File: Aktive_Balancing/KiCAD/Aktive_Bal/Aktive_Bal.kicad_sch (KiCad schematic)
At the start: 60 parts, among them J1 Screw_Terminal_01x02, J10 Conn_01x01_Pin, J11 Conn_01x01_Pin, J2 A-DF_09_A_KG-T4S, J3 Conn_01x02_Pin, J4 Conn_01x02_Pin, J5 Sockel_BluePill, J6 Conn_01x02_Pin, J7 Conn_01x02_Pin, J8 Conn_01x02_Pin, J9 Conn_01x02_Pin, U1 RFP12N10L, U2 SN65HVD233, U3 ADUM1250ARZ-RL7, U4 SCW20C-12, U5 PCA9306DC, U6 EC1SA16N, U7 PCF8575CDB, U8 LM1117IMPX_3_3_NOPB, U9 MCP4725xxx-xCH

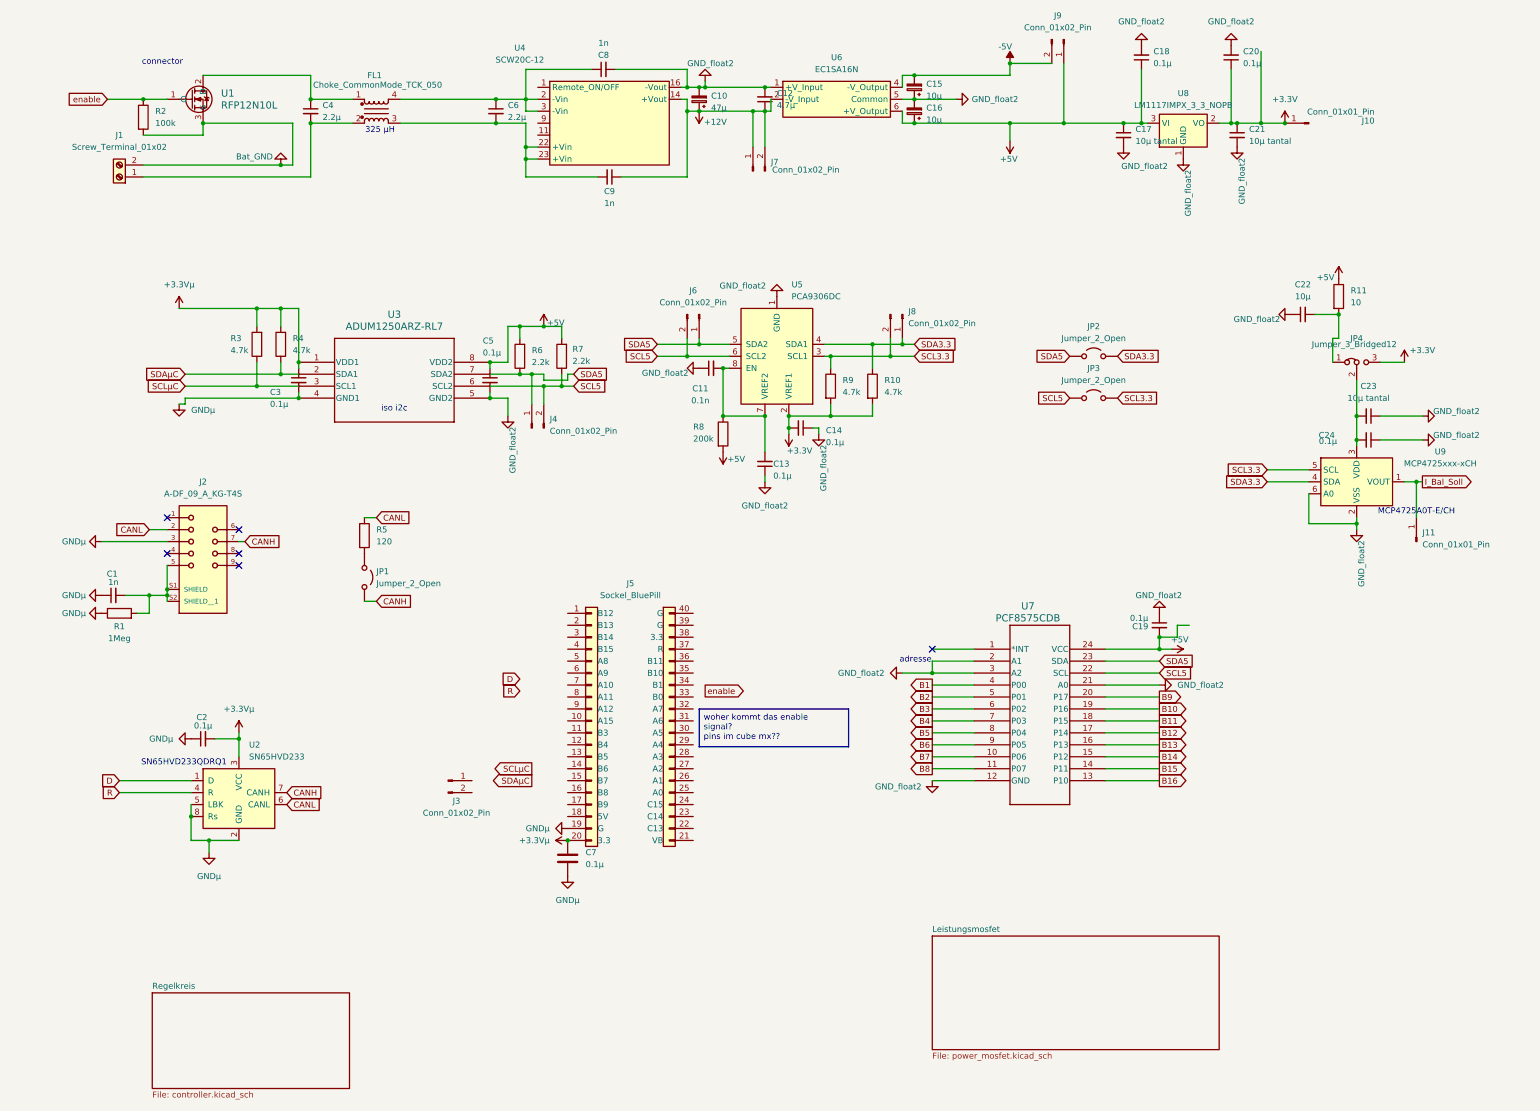
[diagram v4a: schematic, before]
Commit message: layout
Komponenten geordnet
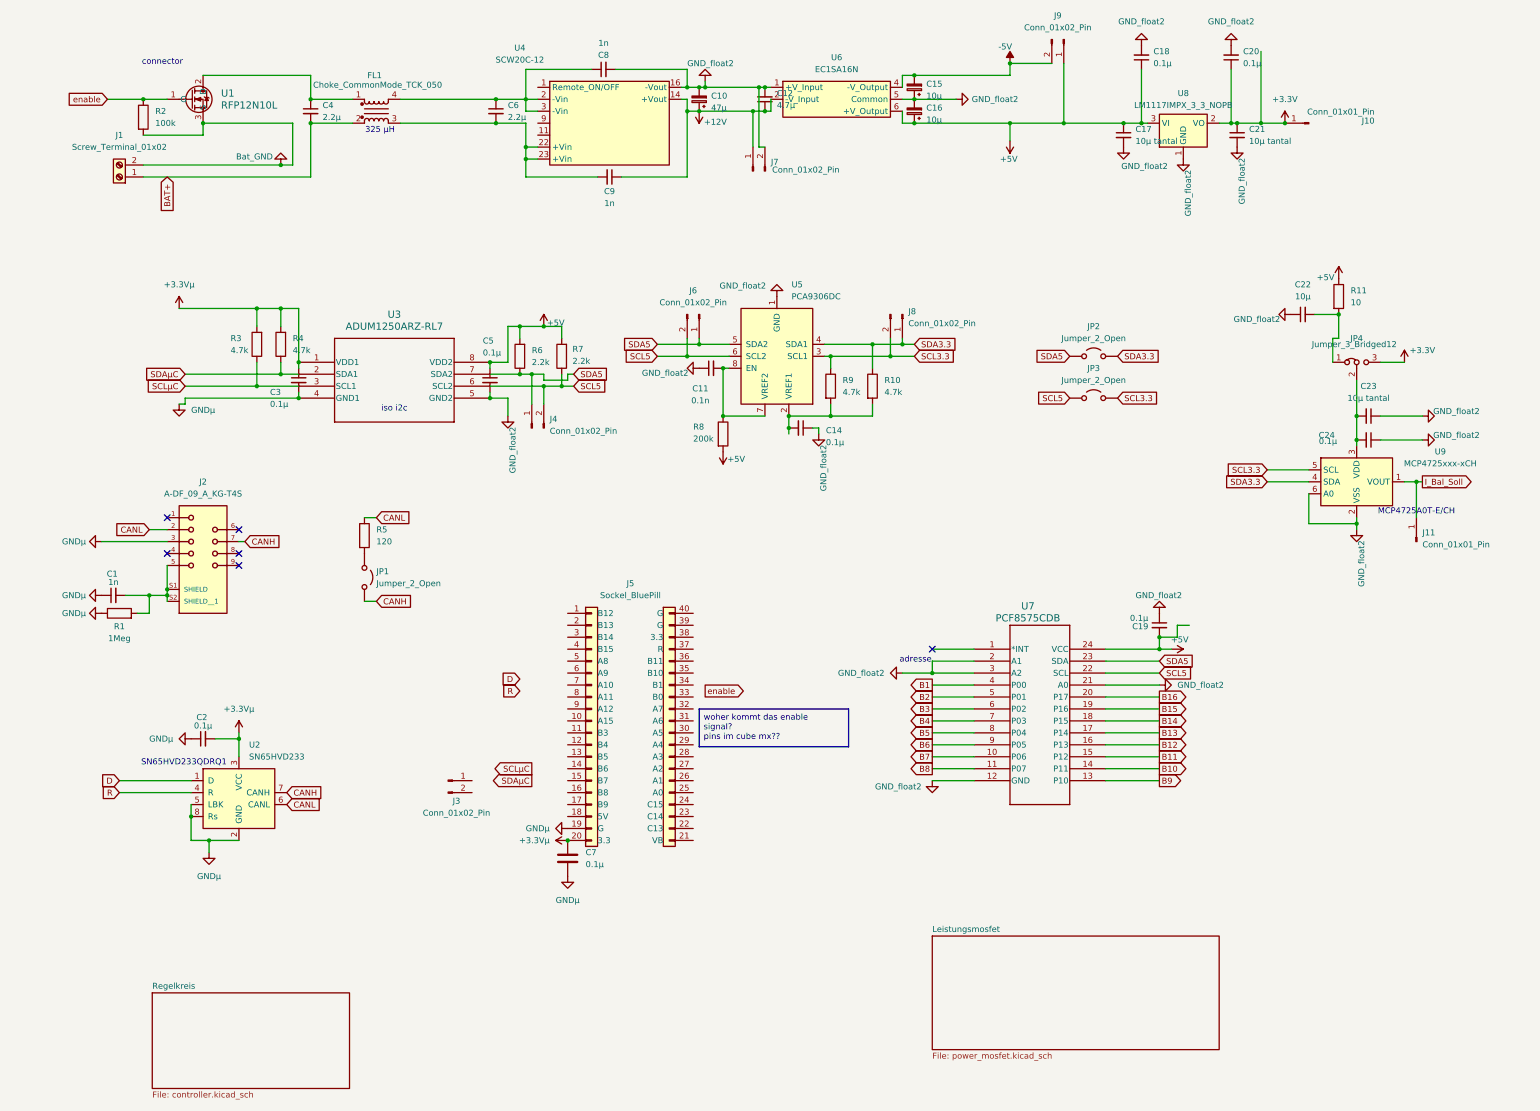
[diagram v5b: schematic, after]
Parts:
- removed C13: 0.1µ, Capacitor_SMD:C_0805_2012Metric, symbol Device:C_Small
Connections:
- net +12V: no longer J7.2 (Pin_2)
- net +3.3V: no longer C14.2, R10.2, R9.2, U5.2 (VREF1)
- net B10: now also U7.14 (P11); no longer U7.19 (P16)
- net B11: now also U7.15 (P12); no longer U7.18 (P15)
- net B12: now also U7.16 (P13); no longer U7.17 (P14)
- net B13: now also U7.17 (P14); no longer U7.16 (P13)
- net B14: now also U7.18 (P15); no longer U7.15 (P12)
- net B15: now also U7.19 (P16); no longer U7.14 (P11)
- net B16: now also U7.20 (P17); no longer U7.13 (P10)
- net B9: now also U7.13 (P10); no longer U7.20 (P17)
- net GND_float2: now also J7.2 (Pin_2)
- net BAT+: now reaches C4.2, FL1.2, J1.1 (Pin_1)
- new net: C14.2, R10.2, R9.2, U5.2 (VREF1)
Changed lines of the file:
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@@
 	)
 	(junction
-		(at 172.72 100.33)
-		(diameter 0)
-		(color 0 0 0 0)
-	)
-	(junction
 		(at 199.39 87.63)
 		(diameter 0)
@@
 		(color 0 0 0 0)
 	)
+	(junction
+		(at 171.45 30.48)
+		(diameter 0)
+		(color 0 0 0 0)
+	)
 	(no_connect
 		(at 45.72 121.92)
@@
 	(wire
 		(pts
-			(xy 172.72 114.3) (xy 172.72 113.03)
-		)
-		(stroke
-			(width 0)
-			(type default)
-		)
-	)
-	(wire
-		(pts
 			(xy 158.75 83.82) (xy 158.75 85.09)
 		)
@@
 	(wire
 		(pts
-			(xy 158.75 30.48) (xy 172.72 30.48)
+			(xy 158.75 30.48) (xy 171.45 30.48)
 		)
 		(stroke
@@
 	(wire
 		(pts
-			(xy 172.72 100.33) (xy 172.72 107.95)
+			(xy 171.45 43.18) (xy 171.45 30.48)
 		)
 		(stroke
@@
 	(wire
 		(pts
+			(xy 171.45 30.48) (xy 172.72 30.48)
+		)
+		(stroke
+			(width 0)
+			(type default)
+		)
+	)
+	(wire
+		(pts
 			(xy 288.29 123.19) (xy 298.45 123.19)
 		)
@@
 	(wire
 		(pts
-			(xy 172.72 35.56) (xy 172.72 43.18)
-		)
-		(stroke
-			(width 0)
-			(type default)
-		)
-	)
-	(wire
-		(pts
 			(xy 49.53 91.44) (xy 69.85 91.44)
 		)
@@
 	(wire
 		(pts
+			(xy 172.72 43.18) (xy 171.45 43.18)
+		)
+		(stroke
+			(width 0)
+			(type default)
+		)
+	)
+	(wire
+		(pts
 			(xy 64.77 88.9) (xy 64.77 93.98)
 		)
@@
 	(global_label "B13"
 		(shape output)
-		(at 256.54 170.18 0)
+		(at 256.54 167.64 0)
 		(fields_autoplaced yes)
 		(effects
@@
 		)
 		(property "Intersheetrefs" "${INTERSHEET_REFS}"
-			(at 263.2142 170.18 0)
+			(at 263.2142 167.64 0)
 			(hide yes)
 			(show_name no)
@@
 	(global_label "B14"
 		(shape output)
-		(at 256.54 172.72 0)
+		(at 256.54 165.1 0)
 		(fields_autoplaced yes)
 		(effects
@@
 		)
 		(property "Intersheetrefs" "${INTERSHEET_REFS}"
-			(at 263.2142 172.72 0)
+			(at 263.2142 165.1 0)
 			(hide yes)
 			(show_name no)
@@
 	(global_label "B12"
 		(shape output)
-		(at 256.54 167.64 0)
+		(at 256.54 170.18 0)
 		(fields_autoplaced yes)
 		(effects
@@
 		)
 		(property "Intersheetrefs" "${INTERSHEET_REFS}"
-			(at 263.2142 167.64 0)
+			(at 263.2142 170.18 0)
 			(hide yes)
 			(show_name no)
@@
 	(global_label "B11"
 		(shape output)
-		(at 256.54 165.1 0)
+		(at 256.54 172.72 0)
 		(fields_autoplaced yes)
 		(effects
@@
 		)
 		(property "Intersheetrefs" "${INTERSHEET_REFS}"
-			(at 263.2142 165.1 0)
+			(at 263.2142 172.72 0)
 			(hide yes)
 			(show_name no)
@@
 		)
 	)
+	(global_label "BAT+"
+		(shape input)
+		(at 45.72 49.53 270)
+		(fields_autoplaced yes)
+		(effects
+			(font
+				(size 1.27 1.27)
+			)
+			(justify right)
+		)
+		(property "Intersheetrefs" "${INTERSHEET_REFS}"
+			(at 45.72 57.4138 90)
+			(hide yes)
+			(show_name no)
+			(do_not_autoplace no)
+			(effects
+				(font
+					(size 1.27 1.27)
+				)
+				(justify right)
+			)
+		)
+	)
 	(global_label "SCL3.3"
 		(shape input)
@@
 	(global_label "B16"
 		(shape output)
-		(at 256.54 177.8 0)
+		(at 256.54 160.02 0)
 		(fields_autoplaced yes)
 		(effects
@@
 		)
 		(property "Intersheetrefs" "${INTERSHEET_REFS}"
-			(at 263.2142 177.8 0)
+			(at 263.2142 160.02 0)
 			(hide yes)
 			(show_name no)
@@
 	(global_label "B15"
 		(shape output)
-		(at 256.54 175.26 0)
+		(at 256.54 162.56 0)
 		(fields_autoplaced yes)
 		(effects
@@
 		)
 		(property "Intersheetrefs" "${INTERSHEET_REFS}"
-			(at 263.2142 175.26 0)
+			(at 263.2142 162.56 0)
 			(hide yes)
 			(show_name no)
@@
 	(global_label "B10"
 		(shape output)
-		(at 256.54 162.56 0)
+		(at 256.54 175.26 0)
 		(fields_autoplaced yes)
 		(effects
@@
 		)
 		(property "Intersheetrefs" "${INTERSHEET_REFS}"
-			(at 263.2142 162.56 0)
+			(at 263.2142 175.26 0)
 			(hide yes)
 			(show_name no)
@@
 	(global_label "B9"
 		(shape output)
-		(at 256.54 160.02 0)
+		(at 256.54 177.8 0)
 		(fields_autoplaced yes)
 		(effects
@@
 		)
 		(property "Intersheetrefs" "${INTERSHEET_REFS}"
-			(at 262.0047 160.02 0)
+			(at 262.0047 177.8 0)
 			(hide yes)
 			(show_name no)
@@
 	)
 	(symbol
-		(lib_id "power:GND")
-		(at 172.72 114.3 0)
-		(unit 1)
-		(body_style 1)
-		(exclude_from_sim no)
-		(in_bom yes)
-		(on_board yes)
-		(in_pos_files yes)
-		(dnp no)
-		(fields_autoplaced yes)
-		(property "Reference" "#PWR019"
-			(at 172.72 120.65 0)
-			(hide yes)
-			(show_name no)
-			(do_not_autoplace no)
-			(effects
-				(font
-					(size 1.27 1.27)
-				)
-			)
-		)
-		(property "Value" "GND_float2"
-			(at 172.72 119.38 0)
-			(show_name no)
-			(do_not_autoplace no)
-			(effects
-				(font
-					(size 1.27 1.27)
-				)
-			)
-		)
-		(property "Footprint" ""
-			(at 172.72 114.3 0)
-			(hide yes)
-			(show_name no)
-			(do_not_autoplace no)
-			(effects
-				(font
-					(size 1.27 1.27)
-				)
-			)
-		)
-		(property "Datasheet" ""
-			(at 172.72 114.3 0)
-			(hide yes)
-			(show_name no)
-			(do_not_autoplace no)
-			(effects
-				(font
-					(size 1.27 1.27)
-				)
-			)
-		)
-		(property "Description" "Power symbol creates a global label with name \"GND\" , ground"
-			(at 172.72 114.3 0)
-			(hide yes)
-			(show_name no)
-			(do_not_autoplace no)
-			(effects
-				(font
-					(size 1.27 1.27)
-				)
-			)
-		)
-		(pin "1"
-		)
-		(instances
-			(project "Aktive_Bal"
-				(path "/7c40c112-cd2b-4a48-9744-14a65613b3b5"
-					(reference "#PWR019")
-					(unit 1)
-				)
-			)
-		)
-	)
-	(symbol
 		(lib_id "Jumper:Jumper_3_Bridged12")
 		(at 298.45 88.9 0)
@@
 	)
 	(symbol
-		(lib_id "power:+3.3V")
-		(at 177.8 104.14 180)
-		(unit 1)
-		(body_style 1)
-		(exclude_from_sim no)
-		(in_bom yes)
-		(on_board yes)
-		(in_pos_files yes)
-		(dnp no)
-		(property "Reference" "#PWR021"
-			(at 177.8 100.33 0)
-			(hide yes)
-			(show_name no)
-			(do_not_autoplace no)
-			(effects
-				(font
-					(size 1.27 1.27)
-				)
-			)
-		)
-		(property "Value" "+3.3V"
-			(at 180.086 107.696 0)
-			(show_name no)
-			(do_not_autoplace no)
-			(effects
-				(font
-					(size 1.27 1.27)
-				)
-			)
-		)
-		(property "Footprint" ""
-			(at 177.8 104.14 0)
-			(hide yes)
-			(show_name no)
-			(do_not_autoplace no)
-			(effects
-				(font
-					(size 1.27 1.27)
-				)
-			)
-		)
-		(property "Datasheet" ""
-			(at 177.8 104.14 0)
-			(hide yes)
-			(show_name no)
-			(do_not_autoplace no)
-			(effects
-				(font
-					(size 1.27 1.27)
-				)
-			)
-		)
-		(property "Description" "Power symbol creates a global label with name \"+3.3V\""
-			(at 177.8 104.14 0)
-			(hide yes)
-			(show_name no)
-			(do_not_autoplace no)
-			(effects
-				(font
-					(size 1.27 1.27)
-				)
-			)
-		)
-		(pin "1"
-		)
-		(instances
-			(project "Aktive_Bal"
-				(path "/7c40c112-cd2b-4a48-9744-14a65613b3b5"
-					(reference "#PWR021")
-					(unit 1)
-				)
-			)
-		)
-	)
-	(symbol
 		(lib_id "Jumper:Jumper_2_Open")
 		(at 242.57 96.52 0)
@@
 					(unit 1)
 				)
-			)
-		)
-	)
-	(symbol
-		(lib_id "Device:C_Small")
-		(at 172.72 110.49 180)
-		(unit 1)
-		(body_style 1)
-		(exclude_from_sim no)
-		(in_bom yes)
-		(on_board yes)
-		(in_pos_files yes)
-		(dnp no)
-		(property "Reference" "C13"
-			(at 174.498 110.4835 0)
-			(show_name no)
-			(do_not_autoplace no)
-			(effects
-				(font
-					(size 1.27 1.27)
-				)
-				(justify right)
-			)
-		)
-		(property "Value" "0.1µ"
-			(at 174.498 113.0235 0)
-			(show_name no)
-			(do_not_autoplace no)
-			(effects
-				(font
-					(size 1.27 1.27)
-				)
-				(justify right)
-			)
-		)
-		(property "Footprint" "Capacitor_SMD:C_0805_2012Metric"
-			(at 172.72 110.49 0)
-			(hide yes)
-			(show_name no)
-			(do_not_autoplace no)
-			(effects
-				(font
-					(size 1.27 1.27)
-				)
-			)
-		)
-		(property "Datasheet" ""
-			(at 172.72 110.49 0)
-			(hide yes)
-			(show_name no)
-			(do_not_autoplace no)
-			(effects
-				(font
-					(size 1.27 1.27)
-				)
-			)
-		)
-		(property "Description" "Unpolarized capacitor, small symbol"
-			(at 172.72 110.49 0)
-			(hide yes)
-			(show_name no)
-			(do_not_autoplace no)
-			(effects
-				(font
-					(size 1.27 1.27)
-				)
-			)
-		)
-		(pin "1"
-		)
-		(pin "2"
-		)
-		(instances
-			(project "Aktive_Bal"
-				(path "/7c40c112-cd2b-4a48-9744-14a65613b3b5"
-					(reference "C13")
-					(unit 1)
-				)

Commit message: Schaltung Review + Layout
Schaltung Review + Layout
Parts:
- removed J10, J11: Conn_01x01_Pin, Connector_PinHeader_2.54mm:PinHeader_1x01_P2.54mm_Vertical, symbol Connector:Conn_01x01_Pin
- added J11, J13, J14, J4, J6: Conn_01x02_Pin, Connector_PinHeader_2.54mm:PinHeader_1x02_P2.54mm_Vertical, symbol Connector:Conn_01x02_Pin
- added JP2, JP3: Jumper_2_Bridged, Connector_PinHeader_2.54mm:PinHeader_1x02_P2.54mm_Vertical, symbol Jumper:Jumper_2_Bridged
- added JP4, JP5, JP8: Jumper_3_Bridged12, Connector_PinHeader_2.54mm:PinHeader_1x03_P2.54mm_Vertical, symbol Jumper:Jumper_3_Bridged12
- renumbered C14 to C13, C15 to C14, C16 to C15, C17 to C16, C18 to C17, C19 to C18, C20 to C19, C3 to C2, C21 to C20, C22 to C21, C23 to C22, C24 to C23, C2 to C3, J8 to J10, J9 to J12, J4 to J5, J5 to J7, J6 to J8, J7 to J9, JP2 to JP6, JP3 to JP7, JP4 to JP9, R3 to R1, R4 to R2, R1 to R3, R2 to R4, U3 to U2, U2 to U3, U6 to U5, U5 to U6
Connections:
- net D is gone; now on net TX: U3.1 (D)
- net R is gone; now on net RX: U3.4 (R)
- net +3.3V: now also C13.2, R10.2, R9.2, U6.2 (VREF1), J13.2 (Pin_2)
- net +3.3Vµ: now also J6.1 (Pin_1)
- net +5V: now also JP4.3 (B), JP5.3 (B)
- net B1: now also J11.2 (Pin_2)
- net CANH: now also J3.2 (Pin_2)
- net CANL: now also J3.1 (Pin_1)
- net GND_float2: now also J11.1 (Pin_1), J13.1 (Pin_1), J14.1 (Pin_1), JP4.1 (A), JP5.1 (A), JP8.1 (A); no longer U7.2 (A1), U7.3 (A2), U9.6 (A0)
- net GNDµ: now also J6.2 (Pin_2)
- net I_Bal_Soll: now also J14.2 (Pin_2)
- net SCL5: now also JP3.1 (A); no longer J8.2 (Pin_2), U6.6 (SCL2)
- net SCLµC: now also J7.14 (B6), J4.2 (Pin_2)
- net SDA5: now also JP2.1 (A); no longer J8.1 (Pin_1), U6.5 (SDA2)
- net SDAµC: now also J7.15 (B7), J4.1 (Pin_1)
- net enable: now also J7.28 (A3)
- net at C22.2, C23.2, JP9.2 (C)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: now also JP8.3 (B)
- net RX: now reaches J7.8 (A11)
- net TX: now reaches J7.9 (A12)
- new net: J8.1 (Pin_1), JP2.2 (B), U6.5 (SDA2)
- new net: JP4.2 (C), U7.2 (A1)
- new net: JP5.2 (C), U7.3 (A2)
- new net: JP8.2 (C), U9.6 (A0)
- new net: J8.2 (Pin_2), JP3.2 (B), U6.6 (SCL2)
- no-connect marks 6 -> 42
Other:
- note added: "Remote on/off SCW20C Offen oder anschluss an Vcc (>2,5V heißt on)"
- note removed: "adresse"
- moved on the sheet: C11, C12, C13, C14, C15, C2, C21, C5, C7, J10, J12, J8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

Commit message: neuer stand
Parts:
- U8: value LM1117IMPX_3_3_NOPB -> LM1117MP-3.3; footprint Aktive_Bal_Footprints:LM1117IMPX-3.3NOPB-DCY0004A_M -> Package_TO_SOT_SMD:SOT-223-3_TabPin2
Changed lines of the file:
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@@
 	)
 	(symbol
+		(lib_id "Regulator_Linear:LM1117MP-3.3")
+		(at 261.62 38.1 0)
+		(unit 1)
+		(body_style 1)
+		(exclude_from_sim no)
+		(in_bom yes)
+		(on_board yes)
+		(in_pos_files yes)
+		(dnp no)
+		(fields_autoplaced yes)
+		(property "Reference" "U8"
+			(at 261.62 31.75 0)
+			(show_name no)
+			(do_not_autoplace no)
+			(effects
+				(font
+					(size 1.27 1.27)
+				)
+			)
+		)
+		(property "Value" "LM1117MP-3.3"
+			(at 261.62 34.29 0)
+			(show_name no)
+			(do_not_autoplace no)
+			(effects
+				(font
+					(size 1.27 1.27)
+				)
+			)
+		)
+		(property "Footprint" "Package_TO_SOT_SMD:SOT-223-3_TabPin2"
+			(at 261.62 38.1 0)
+			(hide yes)
+			(show_name no)
+			(do_not_autoplace no)
+			(effects
+				(font
+					(size 1.27 1.27)
+				)
+			)
+		)
+		(property "Datasheet" "http://www.ti.com/lit/ds/symlink/lm1117.pdf"
+			(at 261.62 38.1 0)
+			(hide yes)
+			(show_name no)
+			(do_not_autoplace no)
+			(effects
+				(font
+					(size 1.27 1.27)
+				)
+			)
+		)
+		(property "Description" "800mA Low-Dropout Linear Regulator, 3.3V fixed output, SOT-223"
+			(at 261.62 38.1 0)
+			(hide yes)
+			(show_name no)
+			(do_not_autoplace no)
+			(effects
+				(font
+					(size 1.27 1.27)
+				)
+			)
+		)
+		(pin "2"
+		)
+		(pin "3"
+		)
+		(pin "1"
+		)
+		(instances
+			(project "Aktive_Bal"
+				(path "/7c40c112-cd2b-4a48-9744-14a65613b3b5"
+					(reference "U8")
+					(unit 1)
+				)
+			)
+		)
+	)
+	(symbol
 		(lib_id "Connector:Conn_01x02_Pin")
 		(at 288.29 40.64 180)
@@
 					(unit 1)
 				)
-			)
-		)
-	)
-	(symbol
-		(lib_id "Regulator_Linear:LM1117MP-3.3")
-		(at 261.62 38.1 0)
-		(unit 1)
-		(body_style 1)
-		(exclude_from_sim no)
-		(in_bom yes)
-		(on_board yes)
-		(in_pos_files yes)
-		(dnp no)
-		(fields_autoplaced yes)
-		(property "Reference" "U8"
-			(at 261.62 31.75 0)
-			(show_name no)
-			(do_not_autoplace no)
-			(effects
-				(font
-					(size 1.27 1.27)
-				)
-			)
-		)
-		(property "Value" "LM1117IMPX_3_3_NOPB"
-			(at 261.62 34.29 0)
-			(show_name no)
-			(do_not_autoplace no)
-			(effects
-				(font
-					(size 1.27 1.27)
-				)
-			)
-		)
-		(property "Footprint" "Aktive_Bal_Footprints:LM1117IMPX-3.3NOPB-DCY0004A_M"
-			(at 261.62 38.1 0)
-			(hide yes)
-			(show_name no)
-			(do_not_autoplace no)
-			(effects
-				(font
-					(size 1.27 1.27)
-				)
-			)
-		)
-		(property "Datasheet" "http://www.ti.com/lit/ds/symlink/lm1117.pdf"
-			(at 261.62 38.1 0)
-			(hide yes)
-			(show_name no)
-			(do_not_autoplace no)
-			(effects
-				(font
-					(size 1.27 1.27)
-				)
-			)
-		)
-		(property "Description" "800mA Low-Dropout Linear Regulator, 3.3V fixed output, SOT-223"
-			(at 261.62 38.1 0)
-			(hide yes)
-			(show_name no)
-			(do_not_autoplace no)
-			(effects
-				(font
-					(size 1.27 1.27)
-				)
-			)
-		)
-		(pin "1"
-		)
-		(pin "2"
-		)
-		(pin "3"
-		)
-		(instances
-			(project "Aktive_Bal"
-				(path "/7c40c112-cd2b-4a48-9744-14a65613b3b5"
-					(reference "U8")
-					(unit 1)
-				)
